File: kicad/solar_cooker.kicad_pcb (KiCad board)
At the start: 2 copper layers, 152.7 x 77.2 mm, 20 parts, among them J1 Pt100, J2 microSD, J3 clock_module, J4 Pt100, J5 BME680, J6 GPS, J7 Pt100, J8 display, U1 anemometer, U2 AM2315C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

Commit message: Electrical Rules Checker fix
there are still some issues that need to be resolved
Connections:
- A1 pad 43: /D43 -> unconnected-(A1-Pad43)
- A1 pad 45: /D45 -> unconnected-(A1-Pad45)
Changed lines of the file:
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@@
   (net 81 "unconnected-(A1-Pad9)")
   (net 82 "unconnected-(A1-Pad10)")
-  (net 83 "/D45")
-  (net 84 "/D43")
+  (net 83 "unconnected-(A1-Pad43)")
+  (net 84 "unconnected-(A1-Pad45)")
   (net 85 "/TX1")
   (net 86 "unconnected-(J6-3.3V-Pad1)")
@@
     (property "Manufacturer" "/")
     (property "SPN" "GPR1206150R")
-    (property "Sheetfile" "solar_cooker_v1.5.kicad_sch")
+    (property "Sheetfile" "solar_cooker.kicad_sch")
     (property "Sheetname" "")
     (property "Supplier" "Eurocircuits")
@@
     (property "Manufacturer" "Molex")
     (property "SPN" "WM9752-ND")
-    (property "Sheetfile" "solar_cooker_v1.5.kicad_sch")
-    (property "Sheetname" "")
+    (property "Sheetfile" "solar_cooker.kicad_sch")
+    (property "Sheetname" "")
+    (property "Sim.Enable" "0")
     (property "Supplier" "Digi-Key")
     (attr through_hole)
@@
     (property "Manufacturer" "Würth Elektronik")
     (property "SPN" "732-4993-1-ND")
-    (property "Sheetfile" "solar_cooker_v1.5.kicad_sch")
-    (property "Sheetname" "")
+    (property "Sheetfile" "solar_cooker.kicad_sch")
+    (property "Sheetname" "")
+    (property "Sim.Enable" "0")
     (property "Supplier" "Digi-Key")
     (property "ki_description" "Light emitting diode")
@@
     (property "Manufacturer" "Samtec Inc.")
     (property "SPN" "SAM1180-07-ND")
-    (property "Sheetfile" "solar_cooker_v1.5.kicad_sch")
-    (property "Sheetname" "")
+    (property "Sheetfile" "solar_cooker.kicad_sch")
+    (property "Sheetname" "")
+    (property "Sim.Enable" "0")
     (property "Supplier" "Digi-Key")
     (attr through_hole)
@@
     (property "Manufacturer" "Everlight Electronics Co Ltd")
     (property "SPN" "1080-1417-2-ND")
-    (property "Sheetfile" "solar_cooker_v1.5.kicad_sch")
-    (property "Sheetname" "")
+    (property "Sheetfile" "solar_cooker.kicad_sch")
+    (property "Sheetname" "")
+    (property "Sim.Enable" "0")
     (property "Supplier" "Digi-Key")
     (property "ki_description" "Light emitting diode")
@@
     (property "Manufacturer" "/")
     (property "SPN" "GPR1206150R")
-    (property "Sheetfile" "solar_cooker_v1.5.kicad_sch")
+    (property "Sheetfile" "solar_cooker.kicad_sch")
     (property "Sheetname" "")
     (property "Supplier" "Eurocircuits")
@@
     (property "Manufacturer" "Samtec Inc.")
     (property "SPN" "SAM1180-09-ND")
-    (property "Sheetfile" "solar_cooker_v1.5.kicad_sch")
-    (property "Sheetname" "")
+    (property "Sheetfile" "solar_cooker.kicad_sch")
+    (property "Sheetname" "")
+    (property "Sim.Enable" "0")
     (property "Supplier" "Digi-Key")
     (attr through_hole)
@@
     (property "Manufacturer" "Samtec Inc.")
     (property "SPN" "SAM1180-08-ND")
-    (property "Sheetfile" "solar_cooker_v1.5.kicad_sch")
-    (property "Sheetname" "")
+    (property "Sheetfile" "solar_cooker.kicad_sch")
+    (property "Sheetname" "")
+    (property "Sim.Enable" "0")
     (property "Supplier" "Digi-Key")
     (attr through_hole)
@@
     (property "Manufacturer" "Samtec Inc.")
     (property "SPN" "SAM1180-08-ND")
-    (property "Sheetfile" "solar_cooker_v1.5.kicad_sch")
-    (property "Sheetname" "")
+    (property "Sheetfile" "solar_cooker.kicad_sch")
+    (property "Sheetname" "")
+    (property "Sim.Enable" "0")
     (property "Supplier" "Digi-Key")
     (attr through_hole)
@@
     (property "Manufacturer" "E-switch")
     (property "SPN" "EG5137-ND")
-    (property "Sheetfile" "solar_cooker_v1.5.kicad_sch")
-    (property "Sheetname" "")
+    (property "Sheetfile" "solar_cooker.kicad_sch")
+    (property "Sheetname" "")
+    (property "Sim.Enable" "0")
     (property "Supplier" "Digi-Key")
     (attr through_hole)
@@
     (property "Manufacturer" "Samtec Inc.")
     (property "SPN" "SAM1180-09-ND")
-    (property "Sheetfile" "solar_cooker_v1.5.kicad_sch")
-    (property "Sheetname" "")
+    (property "Sheetfile" "solar_cooker.kicad_sch")
+    (property "Sheetname" "")
+    (property "Sim.Enable" "0")
     (property "Supplier" "Digi-Key")
     (attr smd)
@@
     (property "Manufacturer" "Traco Power")
     (property "SPN" "1951-3372-ND")
-    (property "Sheetfile" "solar_cooker_v1.5.kicad_sch")
-    (property "Sheetname" "")
+    (property "Sheetfile" "solar_cooker.kicad_sch")
+    (property "Sheetname" "")
+    (property "Sim.Enable" "0")
     (property "Supplier" "Digi-Key")
     (attr through_hole)
@@
     (property "Manufacturer" "Samtec Inc.")
     (property "SPN" "SAM1180-08-ND")
-    (property "Sheetfile" "solar_cooker_v1.5.kicad_sch")
-    (property "Sheetname" "")
+    (property "Sheetfile" "solar_cooker.kicad_sch")
+    (property "Sheetname" "")
+    (property "Sim.Enable" "0")
     (property "Supplier" "Digi-Key")
     (attr through_hole)
@@
     (property "Manufacturer" "/")
     (property "SPN" "GPR120610K")
-    (property "Sheetfile" "solar_cooker_v1.5.kicad_sch")
+    (property "Sheetfile" "solar_cooker.kicad_sch")
     (property "Sheetname" "")
     (property "Supplier" "Eurocircuits")
@@
     (property "Manufacturer" "/")
     (property "SPN" "GPR120610K")
-    (property "Sheetfile" "solar_cooker_v1.5.kicad_sch")
+    (property "Sheetfile" "solar_cooker.kicad_sch")
     (property "Sheetname" "")
     (property "Supplier" "Eurocircuits")
@@
     (property "Manufacturer" "Samtec Inc.")
     (property "SPN" "SAM1180-08-ND")
-    (property "Sheetfile" "solar_cooker_v1.5.kicad_sch")
-    (property "Sheetname" "")
+    (property "Sheetfile" "solar_cooker.kicad_sch")
+    (property "Sheetname" "")
+    (property "Sim.Enable" "0")
     (property "Supplier" "Digi-Key")
     (attr through_hole)
@@
     (property "Manufacturer" "Molex")
     (property "SPN" "WM13967-ND")
-    (property "Sheetfile" "solar_cooker_v1.5.kicad_sch")
-    (property "Sheetname" "")
+    (property "Sheetfile" "solar_cooker.kicad_sch")
+    (property "Sheetname" "")
+    (property "Sim.Enable" "0")
     (property "Supplier" "Digi-Key")
     (attr through_hole)
@@
     (property "Manufacturer" "Samtec Inc.")
     (property "SPN" "SAM1180-08-ND")
-    (property "Sheetfile" "solar_cooker_v1.5.kicad_sch")
-    (property "Sheetname" "")
+    (property "Sheetfile" "solar_cooker.kicad_sch")
+    (property "Sheetname" "")
+    (property "Sim.Enable" "0")
     (property "Supplier" "Digi-Key")
     (attr through_hole)
@@
     (property "Manufacturer" "Molex")
     (property "SPN" "WM13967-ND")
-    (property "Sheetfile" "solar_cooker_v1.5.kicad_sch")
-    (property "Sheetname" "")
+    (property "Sheetfile" "solar_cooker.kicad_sch")
+    (property "Sheetname" "")
+    (property "Sim.Enable" "0")
     (property "Supplier" "Digi-Key")
     (attr through_hole)
@@
   (footprint "A000067:ARDUINO_A000067" (layer "B.Cu")
     (at 183.07 108.9194 90)
-    (property "Sheetfile" "solar_cooker_v1.5.kicad_sch")
-    (property "Sheetname" "")
+    (property "Sheetfile" "solar_cooker.kicad_sch")
+    (property "Sheetname" "")
+    (property "Sim.Enable" "0")
     (property "exclude_from_bom" "")
     (attr through_hole exclude_from_bom)
@@
       (net 45 "unconnected-(A1-Pad42)") (pinfunction "42") (pintype "passive+no_connect"))
     (pad "43" thru_hole circle (at -3.81 -45.72 90) (size 1.358 1.358) (drill 0.85) (layers "*.Cu" "*.Mask")
-      (net 84 "/D43") (pinfunction "43") (pintype "passive"))
+      (net 83 "unconnected-(A1-Pad43)") (pinfunction "43") (pintype "passive+no_connect"))
     (pad "44" thru_hole circle (at -6.35 -43.18 90) (size 1.358 1.358) (drill 0.85) (layers "*.Cu" "*.Mask")
       (net 44 "unconnected-(A1-Pad44)") (pinfunction "44") (pintype "passive+no_connect"))
     (pad "45" thru_hole circle (at -6.35 -45.72 90) (size 1.358 1.358) (drill 0.85) (layers "*.Cu" "*.Mask")
-      (net 83 "/D45") (pinfunction "45") (pintype "passive"))
+      (net 84 "unconnected-(A1-Pad45)") (pinfunction "45") (pintype "passive+no_connect"))
     (pad "46" thru_hole circle (at -8.89 -43.18 90) (size 1.358 1.358) (drill 0.85) (layers "*.Cu" "*.Mask")
       (net 42 "unconnected-(A1-Pad46)") (pinfunction "46") (pintype "passive+no_connect"))

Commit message: kicad 9V DCDC convertor Vout- fix + rename clock
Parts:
- J3: value clock_module -> clock; footprint custom_components:clock_module -> custom_components:clock
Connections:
- PS1 pad 3: unconnected-(PS1--VOUT-Pad3) -> GND
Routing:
- net GND: track 34.9 -> 36.0 mm, vias 40 -> 41
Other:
- board text added: "solar cooker testing station v2.1"
- board text removed: "solar cooker testing station v2"

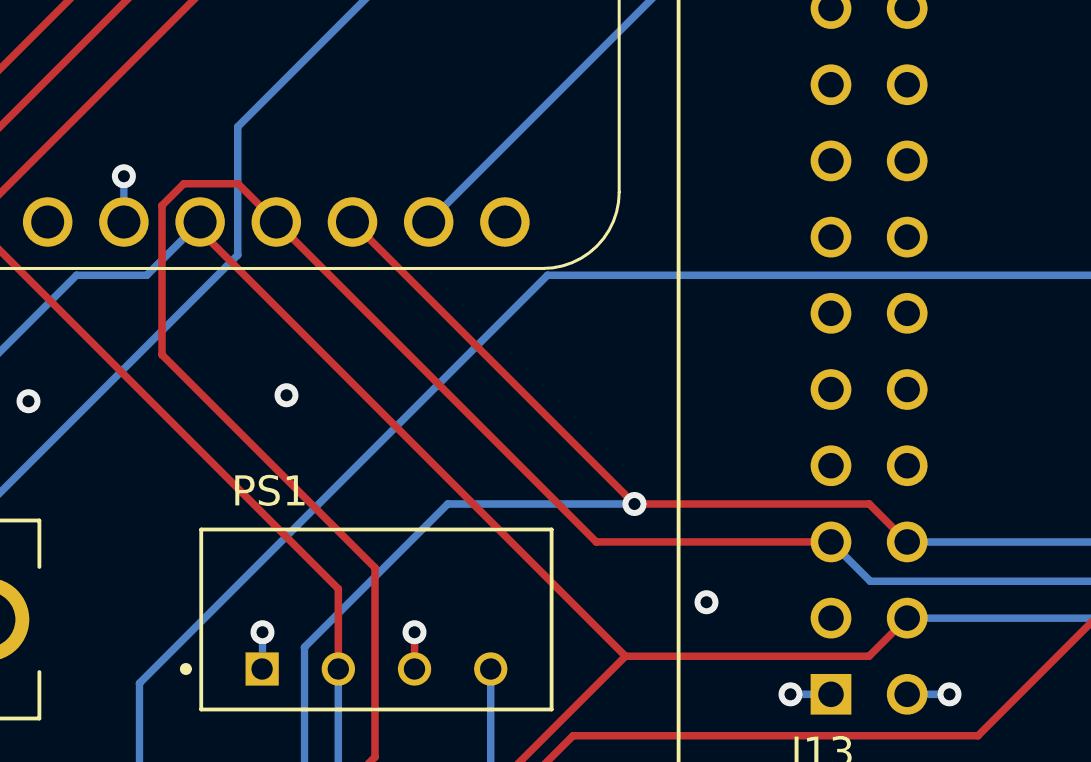
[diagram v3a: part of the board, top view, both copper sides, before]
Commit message: microSD module fix kicad
MISO and MOSI flipped
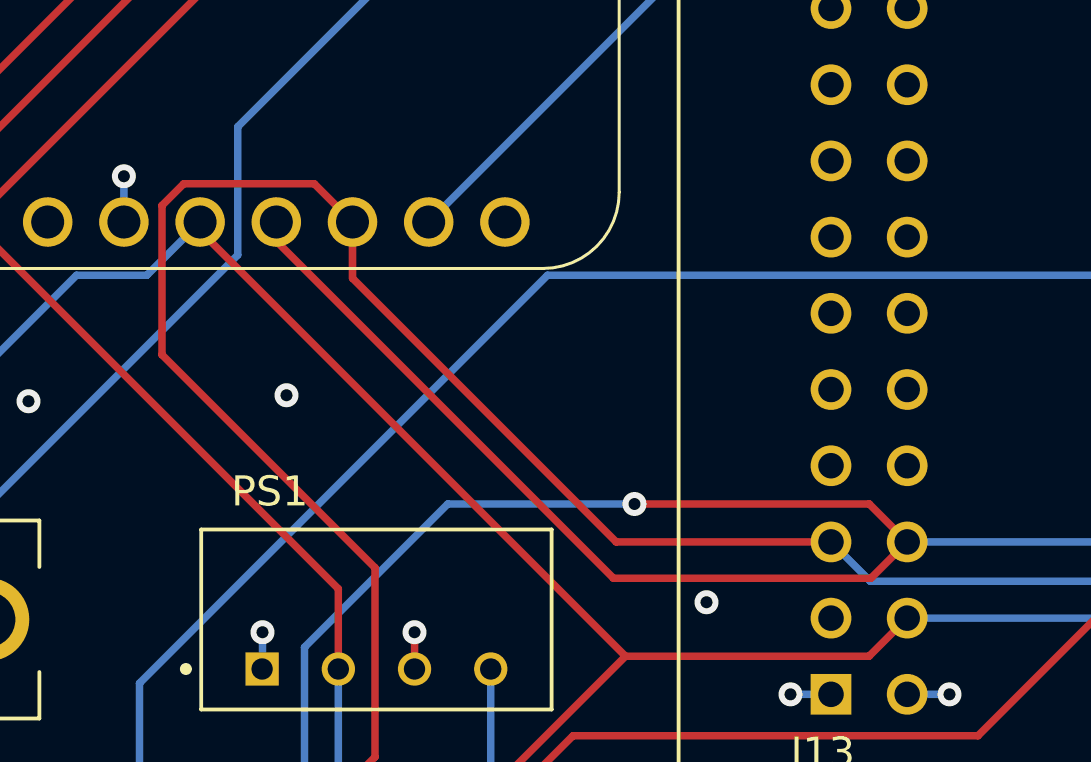
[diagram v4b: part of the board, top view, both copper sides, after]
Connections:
- J2 pad 5: /MOSI -> /MISO
- J2 pad 6: /MISO -> /MOSI
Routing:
- net /MISO: track 229.1 -> 242.6 mm
- net /MOSI: track 238.0 -> 239.1 mm
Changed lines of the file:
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@@
       (net 7 "/SCK") (pinfunction "CLK") (pintype "input"))
     (pad "5" thru_hole circle (at 1.27 14.3256) (size 1.65 1.65) (drill 1.1) (layers "*.Cu" "*.Mask")
-      (net 6 "/MOSI") (pinfunction "DO") (pintype "output"))
+      (net 5 "/MISO") (pinfunction "DO") (pintype "output"))
     (pad "6" thru_hole circle (at 3.81 14.3256) (size 1.65 1.65) (drill 1.1) (layers "*.Cu" "*.Mask")
-      (net 5 "/MISO") (pinfunction "DI") (pintype "input"))
+      (net 6 "/MOSI") (pinfunction "DI") (pintype "input"))
     (pad "7" thru_hole circle (at 6.35 14.3256) (size 1.65 1.65) (drill 1.1) (layers "*.Cu" "*.Mask")
       (net 4 "/D4") (pinfunction "CS") (pintype "input"))
@@
   (segment (start 175.9625 122.9) (end 194.5625 141.5) (width 0.25) (layer "F.Cu") (net 5))
   (segment (start 74.6 117.3) (end 75.1 117.8) (width 0.25) (layer "F.Cu") (net 5))
+  (segment (start 118.86 112.225) (end 118.86 112.861396) (width 0.25) (layer "F.Cu") (net 5))
   (segment (start 165.2 122.9) (end 175.9625 122.9) (width 0.25) (layer "F.Cu") (net 5))
   (segment (start 194.5625 141.5) (end 204.022949 141.5) (width 0.25) (layer "F.Cu") (net 5))
@@
   (segment (start 138.6256 121.625) (end 139.89 122.8894) (width 0.25) (layer "F.Cu") (net 5))
   (segment (start 71.4 126.6) (end 71.4 142.49) (width 0.25) (layer "F.Cu") (net 5))
-  (segment (start 121.4 112.225) (end 130.8 121.625) (width 0.25) (layer "F.Cu") (net 5))
+  (segment (start 118.86 112.861396) (end 130.098604 124.1) (width 0.25) (layer "F.Cu") (net 5))
   (segment (start 74.475 126.225) (end 71.775 126.225) (width 0.25) (layer "F.Cu") (net 5))
+  (segment (start 130.098604 124.1) (end 138.6794 124.1) (width 0.25) (layer "F.Cu") (net 5))
   (segment (start 204.022949 141.5) (end 205.57 139.952949) (width 0.25) (layer "F.Cu") (net 5))
   (segment (start 71.4 142.49) (end 72.775 143.865) (width 0.25) (layer "F.Cu") (net 5))
+  (segment (start 138.6794 124.1) (end 139.89 122.8894) (width 0.25) (layer "F.Cu") (net 5))
   (segment (start 75.1 125.6) (end 74.475 126.225) (width 0.25) (layer "F.Cu") (net 5))
   (via (at 74.6 117.3) (size 0.8) (drill 0.4) (layers "F.Cu" "B.Cu") (net 5))
@@
   (segment (start 205.762949 142.3) (end 208.11 139.952949) (width 0.25) (layer "F.Cu") (net 6))
   (segment (start 194.2 142.3) (end 205.762949 142.3) (width 0.25) (layer "F.Cu") (net 6))
+  (segment (start 176.1 124.2) (end 194.2 142.3) (width 0.25) (layer "F.Cu") (net 6))
   (segment (start 122.15 123.75) (end 115.05 116.65) (width 0.25) (layer "F.Cu") (net 6))
-  (segment (start 176.1 124.2) (end 194.2 142.3) (width 0.25) (layer "F.Cu") (net 6))
   (segment (start 112.256 139.952949) (end 122.15 130.058949) (width 0.25) (layer "F.Cu") (net 6))
+  (segment (start 115.05 111.675) (end 115.775 110.95) (width 0.25) (layer "F.Cu") (net 6))
+  (segment (start 130.1894 122.8894) (end 137.35 122.8894) (width 0.25) (layer "F.Cu") (net 6))
+  (segment (start 115.775 110.95) (end 120.125 110.95) (width 0.25) (layer "F.Cu") (net 6))
+  (segment (start 121.4 114.1) (end 130.1894 122.8894) (width 0.25) (layer "F.Cu") (net 6))
+  (segment (start 121.4 112.225) (end 121.4 114.1) (width 0.25) (layer "F.Cu") (net 6))
+  (segment (start 164.8 124.2) (end 176.1 124.2) (width 0.25) (layer "F.Cu") (net 6))
+  (segment (start 120.125 110.95) (end 121.4 112.225) (width 0.25) (layer "F.Cu") (net 6))
   (segment (start 115.05 116.65) (end 115.05 111.675) (width 0.25) (layer "F.Cu") (net 6))
-  (segment (start 115.05 111.675) (end 115.775 110.95) (width 0.25) (layer "F.Cu") (net 6))
-  (segment (start 115.775 110.95) (end 117.585 110.95) (width 0.25) (layer "F.Cu") (net 6))
-  (segment (start 164.8 124.2) (end 176.1 124.2) (width 0.25) (layer "F.Cu") (net 6))
-  (segment (start 117.585 110.95) (end 118.86 112.225) (width 0.25) (layer "F.Cu") (net 6))
   (segment (start 122.15 130.058949) (end 122.15 123.75) (width 0.25) (layer "F.Cu") (net 6))
-  (segment (start 118.86 112.225) (end 129.5244 122.8894) (width 0.25) (layer "F.Cu") (net 6))
-  (segment (start 129.5244 122.8894) (end 137.35 122.8894) (width 0.25) (layer "F.Cu") (net 6))
   (via (at 165.2 124.2) (size 0.8) (drill 0.4) (layers "F.Cu" "B.Cu") (net 6))
   (segment (start 71.4 139.95) (end 72.775 141.325) (width 0.25) (layer "B.Cu") (net 6))
